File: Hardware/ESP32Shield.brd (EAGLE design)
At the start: 61 x 68.6 mm, 60 parts, among them J2 RJ45, J3 XLR-3-FEMALE, J4 XLR-3-MALE, U1 MAX3485CSA, U2 TXB0104

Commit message: post review changes
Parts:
- removed U$2: 6N137S, SparkFun-DiscreteSemi:8-SMD
- removed U$4: RFB-0505S, SparkFun-IC-Power:RFB-0505S
- added FD1, FD2, FD3, FD4: FIDUCIALUFIDUCIAL, SparkFun-Aesthetics:FIDUCIAL-MICRO
- added R10: 0, SparkFun-Resistors:0603
- added TP1, TP2, TP3, TP4: TEST-POINT3, SparkFun-Connectors:PAD.03X.03
- added U$16: (no value), buzzard_labels (11):#0
- added U$25: (no value), buzzard_labels (11):#1
- added U3, U4, U5: 6N137S, SparkFun-DiscreteSemi:8-SMD
- added U6: RFB-0505S, SparkFun-IC-Power:RFB-0505S
- R1: value 100 -> DNP
- U$1: value 6N137S -> (none); device SparkFun-DiscreteSemi:8-SMD -> buzzard_labels (13):XLR1
- U$3: value 6N137S -> (none); device SparkFun-DiscreteSemi:8-SMD -> buzzard_labels (13):RJ450
- moved U$3 42.2 mm to (29.8, 56.9), turned to 0 degrees
- moved U$1 29.7 mm to (30.0, 55.0), turned to 0 degrees
- moved LOGO2 21.8 mm to (30.5, 45.7)
- moved D1 19.1 mm to (46.4, 24.1)
- moved D2 19.1 mm to (43.8, 24.1)
- moved D3 19.1 mm to (36.8, 55.9)
- moved J2 19.1 mm to (50.2, 55.9)
- moved J3 19.1 mm to (48.3, 12.4)
- moved J4 19.1 mm to (52.1, 35.4)
- moved J7 19.1 mm to (39.4, 29.2)
- moved JP2 19.1 mm to (34.3, 55.9)
- moved R2 19.1 mm to (34.3, 53.3)
- moved R6 19.1 mm to (29.8, 40.0)
- moved U$13 19.1 mm to (54.4, 66.0)
- moved C1 19.1 mm to (24.1, 29.2)
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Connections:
- net 485/TX: now also U3.6; no longer U$1.6
- net 5V: now also U3.8, U4.2, U5.2, U6.1; no longer U$1.8, U$2.2, U$3.2, U$4.1
- net GND: now also R10.2, U3.5, U6.2; no longer U$1.5, U$4.2
- net GND-ISO: now also R10.1, U4.5, U5.5, U6.4; no longer U$2.5, U$3.5, U$4.4
- net HV-DATA1: now also TP1.P$1
- net HV-DATA2: now also TP2.P$1
- net HV-DATA3: now also TP3.P$1
- net HV-LED-CLOCK: now also TP4.P$1
- net N$1: now also U5.3; no longer U$3.3
- net N$2: now also U4.3; no longer U$2.3
- net N$3: now also U4.6; no longer U$2.6
- net N$4: now also U5.6; no longer U$3.6
- net N$5: now also U3.3; no longer U$1.3
- net VCC-ISO: now also U3.2, U4.8, U5.8, U6.6; no longer U$1.2, U$2.8, U$3.8, U$4.6
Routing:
- net 5V: track 162.4 -> 174.6 mm
- net HV-DATA3: track 26.0 -> 30.6 mm, vias 2 -> 3
- net HV-DATA2: track 42.7 -> 46.8 mm, vias 0 -> 1
- net HV-DATA1: track 28.9 -> 32.8 mm, vias 0 -> 1
- net HV-LED-CLOCK: track 84.8 -> 87.3 mm
- net N$3: track 46.6 -> 46.0 mm
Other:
- board text added: "Stop, Drop, Shut 'em down, Open up shop"

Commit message: QC changes
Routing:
- net N$8: track 17.8 -> 18.7 mm
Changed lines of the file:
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@@
 <contactref element="D4" pad="A"/>
 <wire x1="41.275" y1="52.705" x2="39.116" y2="52.705" width="0.2032" layer="16"/>
-<wire x1="33.782" y1="58.039" x2="26.67" y2="58.039" width="0.2032" layer="16"/>
-<via x="26.67" y="58.039" extent="1-16" drill="0.381"/>
-<wire x1="26.67" y1="58.039" x2="26.67" y2="57.03" width="0.2032" layer="1"/>
-<wire x1="39.116" y1="52.705" x2="33.782" y2="58.039" width="0.2032" layer="16"/>
+<wire x1="33.147" y1="58.674" x2="26.67" y2="58.674" width="0.2032" layer="16"/>
+<via x="26.67" y="58.674" extent="1-16" drill="0.381"/>
+<wire x1="26.67" y1="58.674" x2="26.67" y2="57.03" width="0.2032" layer="1"/>
+<wire x1="39.116" y1="52.705" x2="33.147" y2="58.674" width="0.2032" layer="16"/>
 </signal>
 <signal name="N$9">

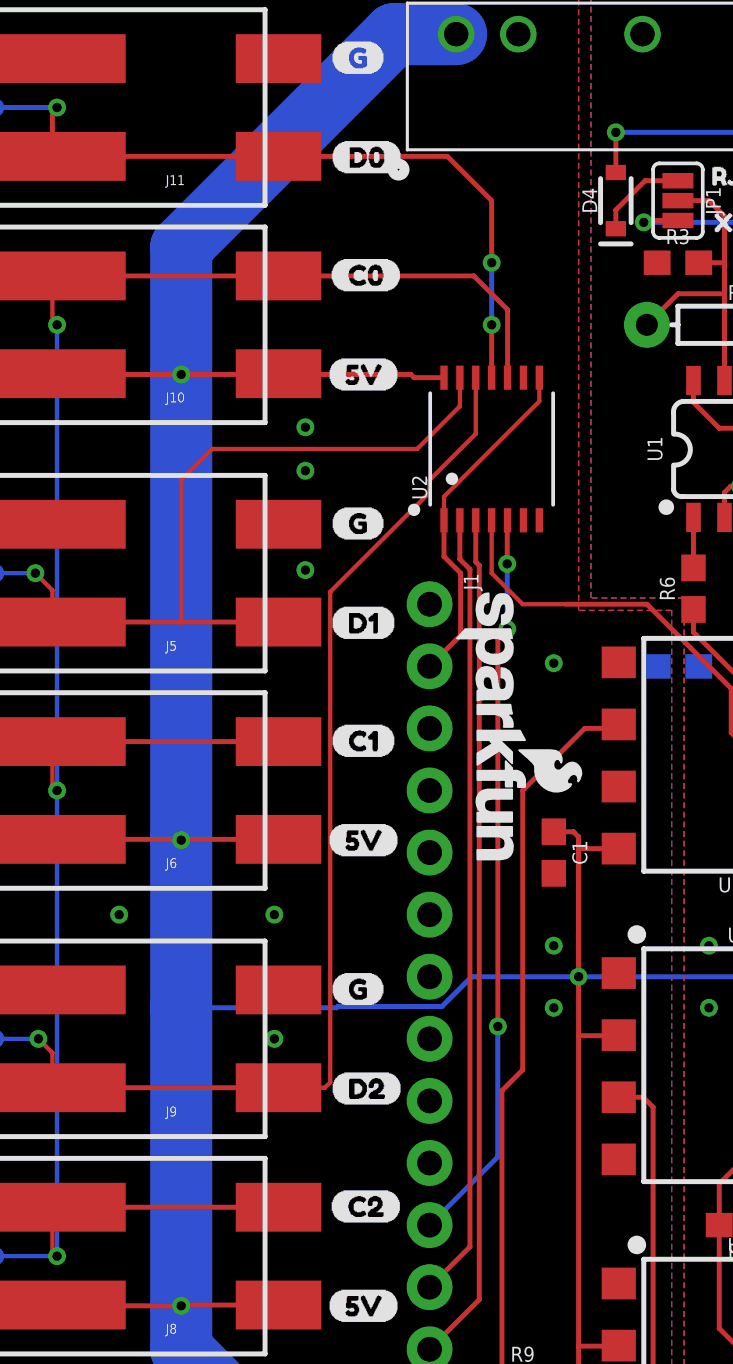
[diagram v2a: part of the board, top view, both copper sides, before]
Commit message: adding beginning of example code
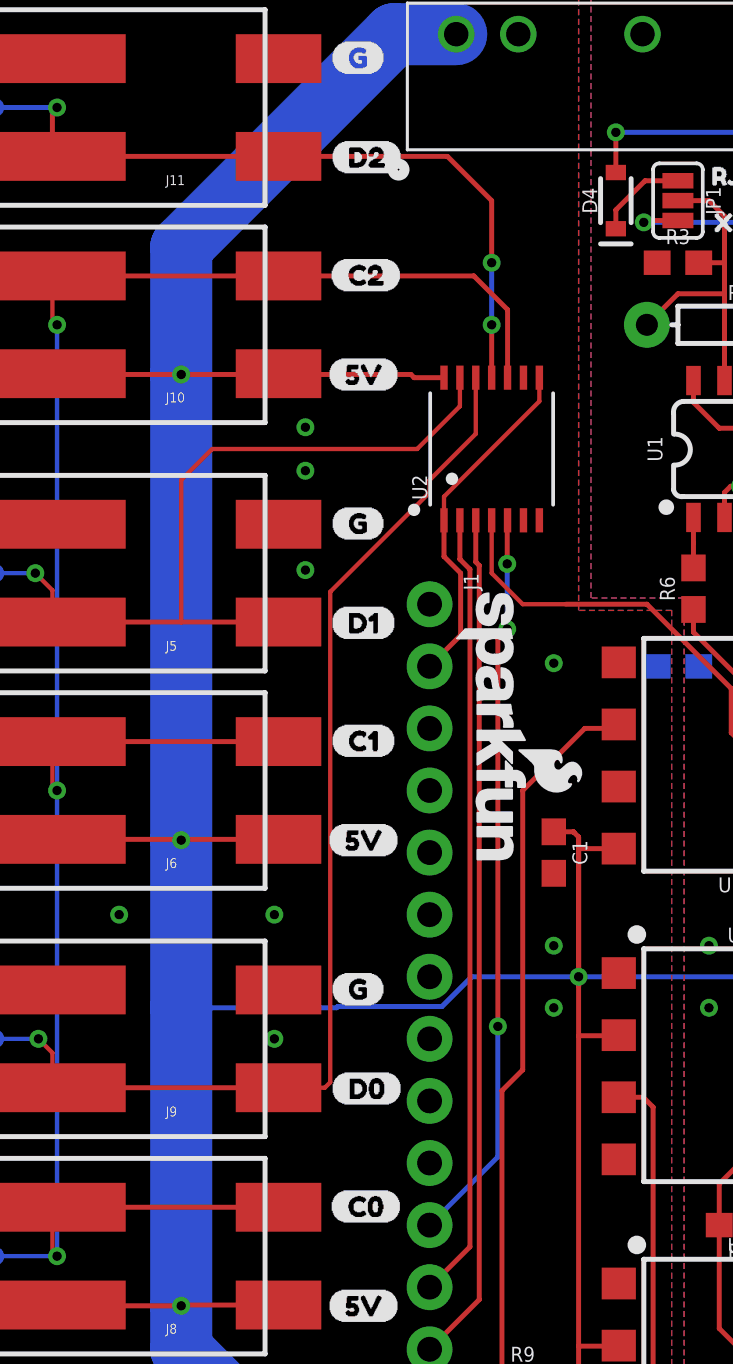
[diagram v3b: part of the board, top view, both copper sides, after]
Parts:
- moved U$18 38.1 mm to (15.0, 14.7)
- moved U$19 38.1 mm to (15.0, 19.6)
- moved U$26 38.1 mm to (15.0, 52.8)
- moved U$27 38.1 mm to (15.0, 57.7)
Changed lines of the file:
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@@
 <element name="U$15" library="buzzard_labels (6)" package="5V7" value="" x="14.859" y="48.768"/>
 <element name="U$17" library="buzzard_labels (6)" package="5V7" value="" x="14.859" y="10.668"/>
-<element name="U$18" library="buzzard_labels (6)" package="C01" value="" x="14.986" y="52.832"/>
-<element name="U$19" library="buzzard_labels (6)" package="D00" value="" x="14.986" y="57.658"/>
+<element name="U$18" library="buzzard_labels (6)" package="C01" value="" x="14.986" y="14.732"/>
+<element name="U$19" library="buzzard_labels (6)" package="D00" value="" x="14.986" y="19.558"/>
 <element name="U$20" library="buzzard_labels (6)" package="G8" value="" x="14.986" y="61.722"/>
 <element name="U$21" library="buzzard_labels (6)" package="5V7" value="" x="14.859" y="29.718"/>
@@
 <element name="U$23" library="buzzard_labels (6)" package="D16" value="" x="14.986" y="38.608"/>
 <element name="U$24" library="buzzard_labels (6)" package="G8" value="" x="14.986" y="42.672"/>
-<element name="U$26" library="buzzard_labels (6)" package="C24" value="" x="14.986" y="14.732"/>
-<element name="U$27" library="buzzard_labels (6)" package="D23" value="" x="14.986" y="19.558"/>
+<element name="U$26" library="buzzard_labels (6)" package="C24" value="" x="14.986" y="52.832"/>
+<element name="U$27" library="buzzard_labels (6)" package="D23" value="" x="14.986" y="57.658"/>
 <element name="U$28" library="buzzard_labels (6)" package="G8" value="" x="14.986" y="23.622"/>
 <element name="LOGO1" library="SparkFun-Aesthetics" package="SFE_LOGO_NAME_FLAME_.1" value="SFE_LOGO_NAME_FLAME.1_INCH" x="21.59" y="34.29" rot="R270"/>

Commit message: updating for reds
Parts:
- removed D1, D2, D3, D4: 3A/10V/280mV, SparkFun-DiscreteSemi:SOD-323
- removed J2: RJ45, SparkFun-Connectors:RJ45-8
- removed JP1, JP2: JUMPER-SMT_3_1-NC_PASTE_SILK, SparkFun-Jumpers:SMT-JUMPER_3_1-NC_PASTE_SILK
- removed R10: 0, SparkFun-Resistors:0603
- removed U$1: (no value), buzzard_labels (13):XLR1
- removed U$3: (no value), buzzard_labels (13):RJ450
- LOGO1, LOGO2: value SFE_LOGO_NAME_FLAME.1_INCH -> SFE_LOGO_NAME_FLAME.2_INCH; device SparkFun-Aesthetics:SFE_LOGO_NAME_FLAME_.1 -> SparkFun-Aesthetics:SFE_LOGO_NAME_FLAME_.2
- moved LOGO1 37.8 mm to (49.5, 59.7), turned to 0 degrees
- moved U$11 31.6 mm to (36.2, 54.6)
- moved U$12 15.9 mm to (36.2, 52.1)
- moved LOGO2 8.89 mm to (30.5, 54.6)
- moved R3 2.84 mm to (30.5, 55.9), turned to 270 degrees
- moved R2 2.84 mm to (33.0, 55.9), turned to 90 degrees
- moved C2 1.27 mm to (35.6, 47.0), turned to 90 degrees
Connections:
- removed net A-XLR: D1.C, J4.2, JP1.3
- removed net B-XLR: D2.C, J4.3, JP2.3
- removed net N$10: D2.A, J3.3
- removed net N$11: D4.C, JP1.1
- removed net N$12: D3.C, JP2.1
- removed net N$7: D3.A, J2.1
- removed net N$8: D4.A, J2.2
- removed net N$9: D1.A, J3.2
- net A: now also J3.3, J4.3; no longer JP2.2
- net B: now also J3.2, J4.2; no longer JP1.2
- net GND: no longer R10.2
- net GND-ISO: no longer R10.1
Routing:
- net B: track 13.6 -> 65.3 mm
- net A-XLR: track 42.4 -> 0.00 mm, vias 1 -> 0
- net A: track 13.6 -> 55.4 mm
- net B-XLR: track 37.8 -> 0.00 mm, vias 1 -> 0
- net N$8: track 18.7 -> 0.00 mm, vias 1 -> 0
- net N$9: track 15.6 -> 0.00 mm
- net N$10: track 10.5 -> 0.00 mm
- net N$7: track 9.83 -> 0.00 mm, vias 1 -> 0
- net N$12: track 3.80 -> 0.00 mm
- net N$11: track 3.80 -> 0.00 mm
- net N$3: track 46.0 -> 42.5 mm
- net VCC-ISO: track 79.6 -> 80.6 mm
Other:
- board text removed: "Stop, Drop, Shut 'em down, Open up shop"

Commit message: post checklist changes
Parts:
- added U$1: (no value), buzzard_labels (1):__TERM__0
- J1: device SparkFun-Connectors:1X16_NO_SILK -> SparkFun-Connectors:1X16_LOCK_NO_SILK
- J7: device SparkFun-Connectors:1X12_NO_SILK -> SparkFun-Connectors:1X12_LOCK_NO_SILK
- moved C1 37.0 mm to (21.0, 66.0), turned to 0 degrees
- moved J1 19.0 mm to (19.1, 20.3)
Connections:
- net 3.3V: now also R9.2, U3.8, U4.2, U5.2
- net 5V: no longer R9.2, U3.8, U4.2, U5.2
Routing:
- net 3.3V: track 14.2 -> 51.7 mm, vias 0 -> 1
- net 5V: track 174.6 -> 137.4 mm, vias 4 -> 3
- net 485/TX: track 33.0 -> 34.1 mm
- net A: track 55.4 -> 56.4 mm
- net VCC-ISO: track 80.6 -> 79.7 mm
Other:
- board text added: "v10"
- board text removed: "v01"

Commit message: a few unsaved changes
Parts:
- added U$2: (no value), buzzard_labels (1):__TERM__0
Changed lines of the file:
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@@
 <setting verticaltext="up"/>
 </settings>
-<grid distance="1" unitdist="mm" unit="mm" style="lines" multiple="1" display="yes" altdistance="0.1" altunitdist="mm" altunit="mm"/>
+<grid distance="0.05" unitdist="inch" unit="inch" style="lines" multiple="1" display="yes" altdistance="0.01" altunitdist="inch" altunit="inch"/>
 <layers>
 <layer number="1" name="Top" color="4" fill="1" visible="yes" active="yes"/>
@@
 <element name="TP4" library="SparkFun-Connectors" package="PAD.03X.03" value="TEST-POINT3" x="1.27" y="12.7" rot="MR0"/>
 <element name="U$1" library="buzzard_labels (1)" package="__TERM__0" value="" x="28.448" y="50.8"/>
+<element name="U$2" library="buzzard_labels (1)" package="__TERM__0" value="" x="35.052" y="50.8" rot="MR0"/>
 </elements>
 <signals>
@@
 <vertex x="0" y="68.58"/>
 <vertex x="25.146" y="68.58"/>
-<vertex x="25.146" y="43.18"/>
-<vertex x="28.956" y="39.37"/>
+<vertex x="25.146" y="41.148"/>
+<vertex x="28.956" y="37.338"/>
 <vertex x="28.956" y="0"/>
 <vertex x="0" y="0"/>
@@
 <vertex x="0" y="68.58"/>
 <vertex x="25.146" y="68.58"/>
-<vertex x="25.146" y="43.18"/>
-<vertex x="28.956" y="39.37"/>
+<vertex x="25.146" y="41.148"/>
+<vertex x="28.956" y="37.338"/>
 <vertex x="28.956" y="0"/>
 <vertex x="0" y="0"/>
@@
 <vertex x="60.96" y="68.58"/>
 <vertex x="25.654" y="68.58"/>
-<vertex x="25.654" y="43.434"/>
-<vertex x="29.464" y="39.624"/>
+<vertex x="25.654" y="41.402"/>
+<vertex x="29.464" y="37.592"/>
 <vertex x="29.464" y="0"/>
 <vertex x="60.96" y="0"/>
@@
 <vertex x="60.96" y="68.58"/>
 <vertex x="25.654" y="68.58"/>
-<vertex x="25.654" y="43.434"/>
-<vertex x="29.464" y="39.624"/>
+<vertex x="25.654" y="41.402"/>
+<vertex x="29.464" y="37.592"/>
 <vertex x="29.464" y="0"/>
 <vertex x="60.96" y="0"/>
@@
 <wire x1="14.986" y1="19.812" x2="14.764" y2="19.59" width="0.1778" layer="1"/>
 <wire x1="14.764" y1="19.59" x2="12.87" y2="19.59" width="0.1778" layer="1"/>
-<wire x1="14.986" y1="19.812" x2="14.986" y2="39.878" width="0.1778" layer="1"/>
-<wire x1="14.986" y1="39.878" x2="19.05" y2="43.942" width="0.1778" layer="1"/>
-<wire x1="19.05" y1="43.942" x2="19.05" y2="44.45" width="0.1778" layer="1"/>
+<wire x1="14.986" y1="19.812" x2="14.986" y2="40.386" width="0.1778" layer="1"/>
+<wire x1="14.986" y1="40.386" x2="20.94" y2="46.34" width="0.1778" layer="1"/>
 <wire x1="20.94" y1="46.34" x2="20.94" y2="48.6378" width="0.1778" layer="1"/>
-<wire x1="19.05" y1="44.45" x2="20.94" y2="46.34" width="0.1778" layer="1"/>
 <contactref element="TP2" pad="P$1"/>
 <wire x1="3.62" y1="19.59" x2="3.62" y2="21.018" width="0.1778" layer="1"/>
